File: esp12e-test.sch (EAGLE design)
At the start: 12 parts, among them IC1 ESP-12E/F, U8 NCP1117LPST50T3G

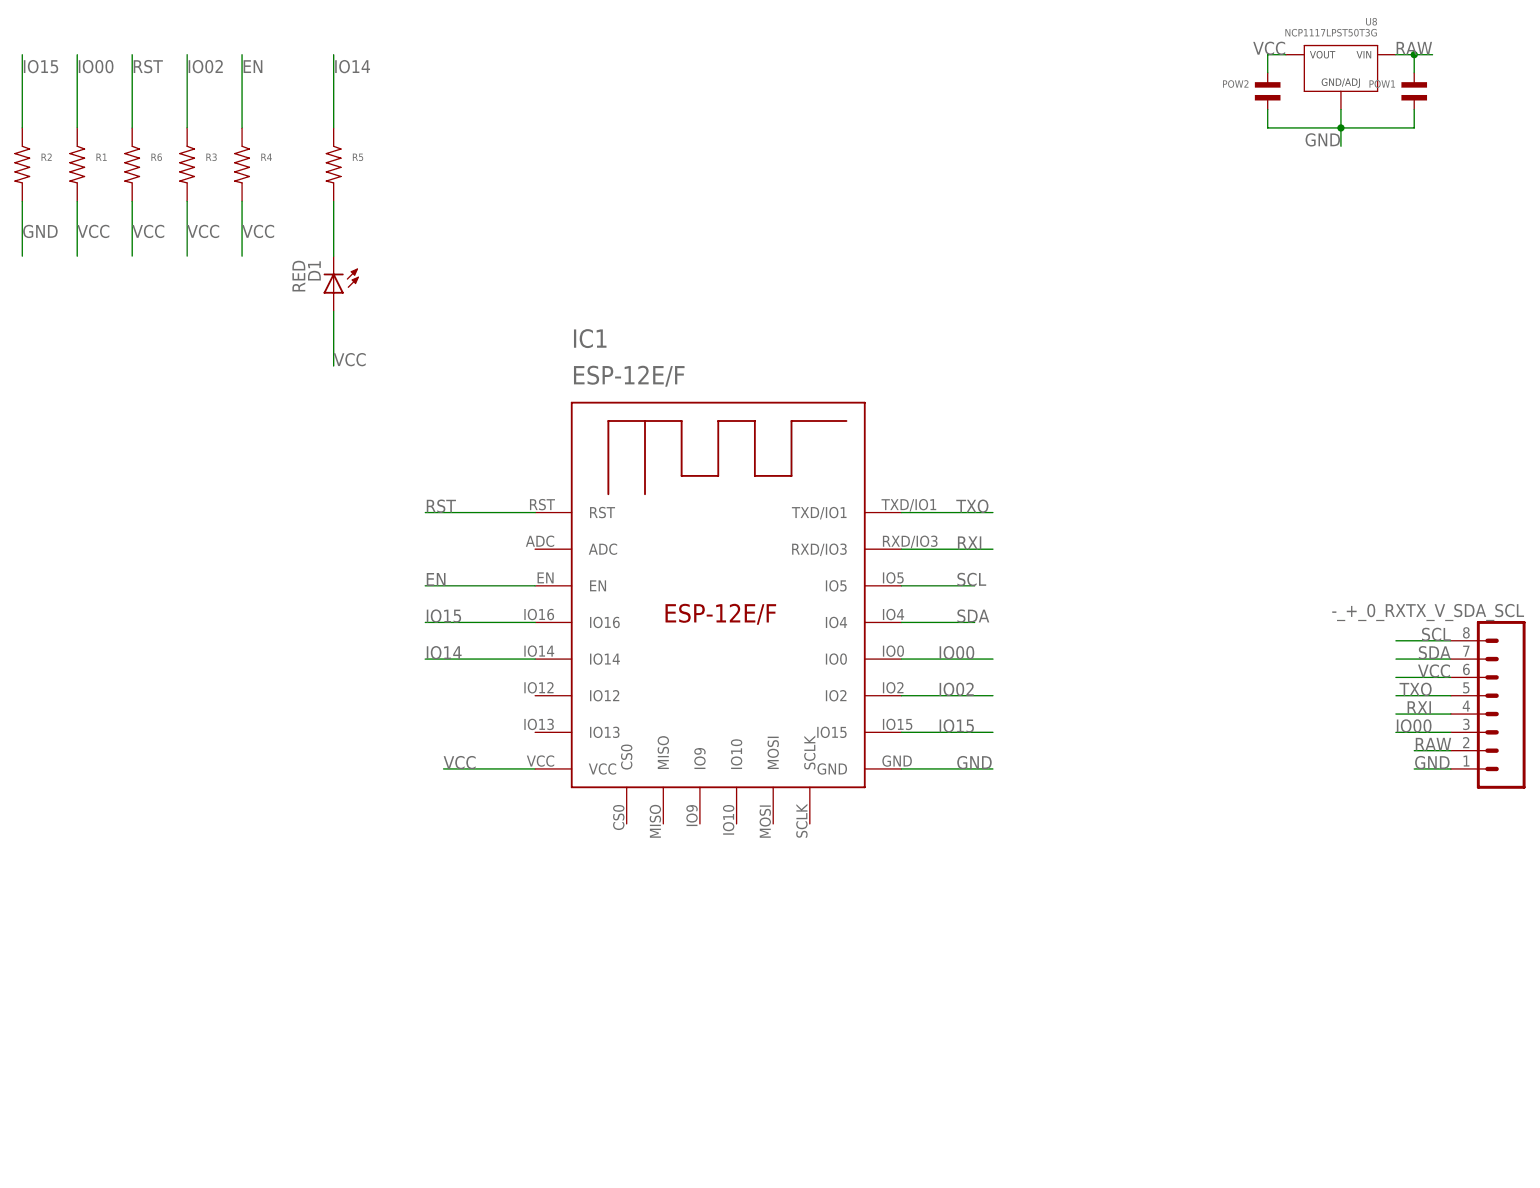
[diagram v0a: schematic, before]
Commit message: Add button and STEMMA connectors to esp12e-test board
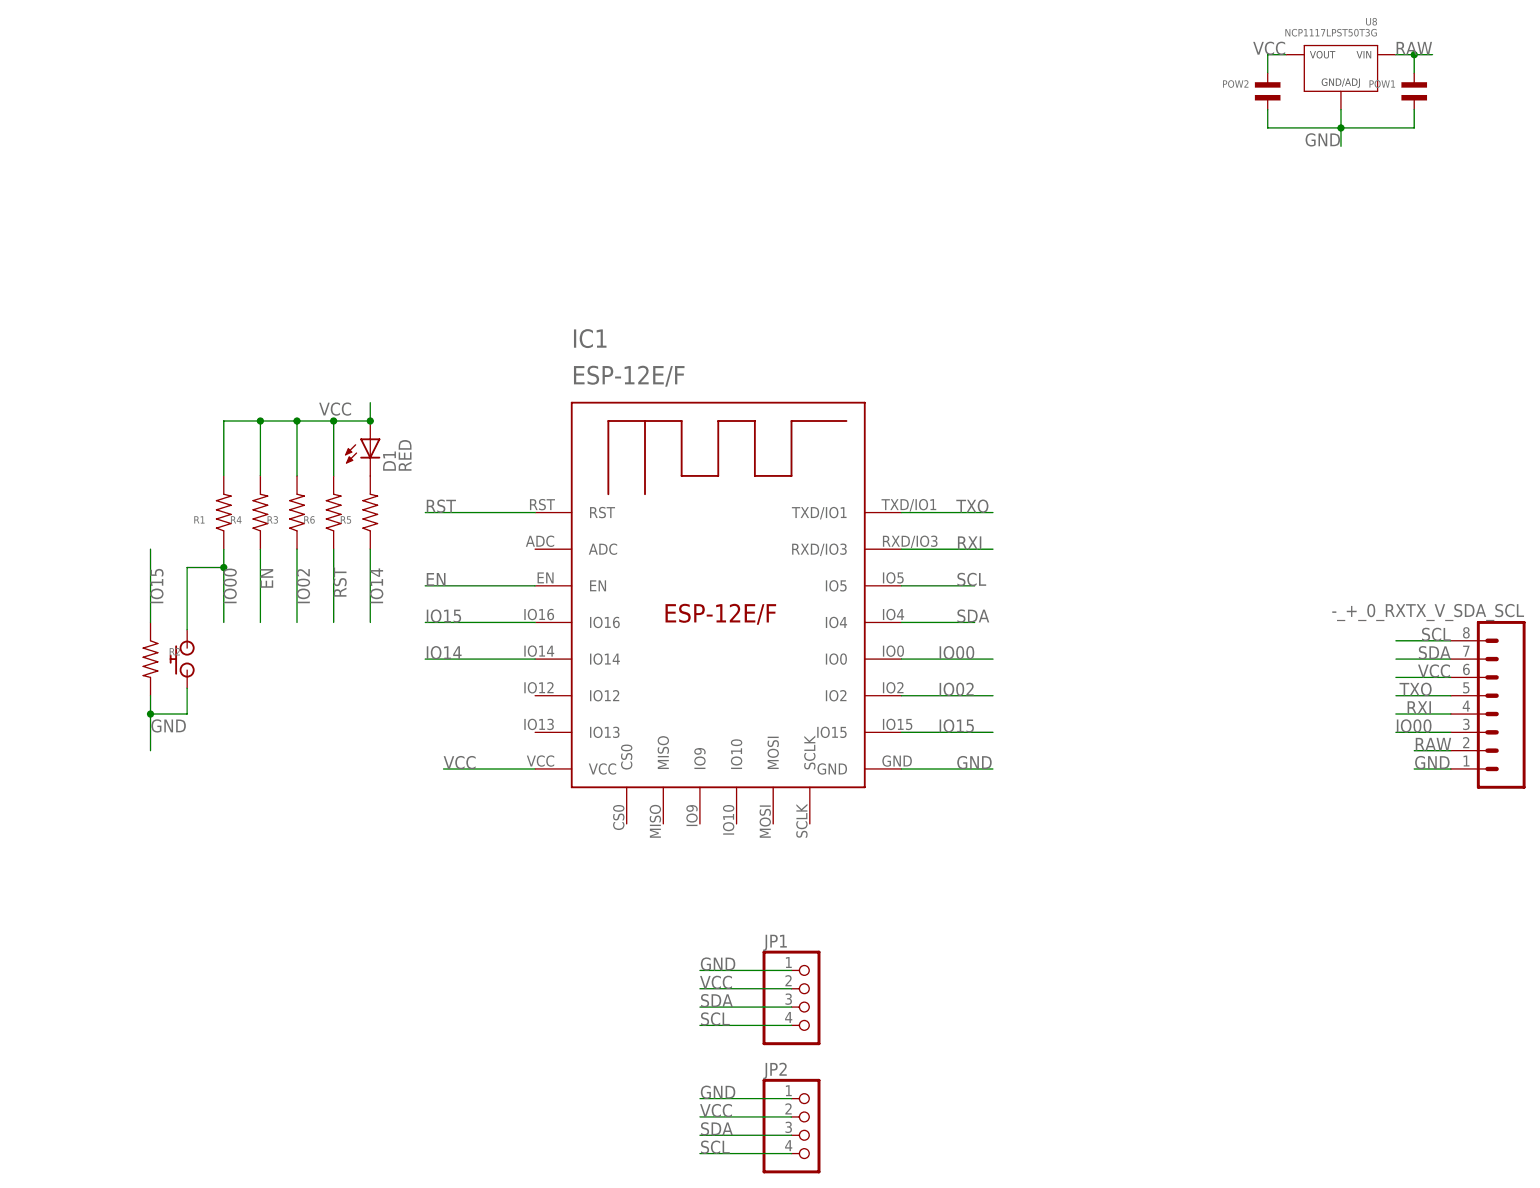
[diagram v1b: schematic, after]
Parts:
- added JP1, JP2: (no value), microbuilder:HEADER-1X41MMPADS
- added U$1: AMAZON_BUTTON, 00jim:AMAZON_BUTTON
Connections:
- net GND: now also JP1.1, JP2.1, U$1.P$2
- net IO00: now also U$1.P$1
- net SCL: now also JP1.4, JP2.4
- net SDA: now also JP1.3, JP2.3
- net VCC: now also JP1.2, JP2.2
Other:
- moved on the sheet: D1, R1, R2, R3, R4, R5, R6
